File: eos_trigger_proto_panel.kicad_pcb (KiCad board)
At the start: 2 copper layers, 69.5 x 37.6 mm, 66 parts, among them J1 Conn_01x02, J2 Conn_01x02, J3 Conn_01x03, J4 Conn_01x02, U4 SMA-Mylibrary, U5 SMA-Mylibrary

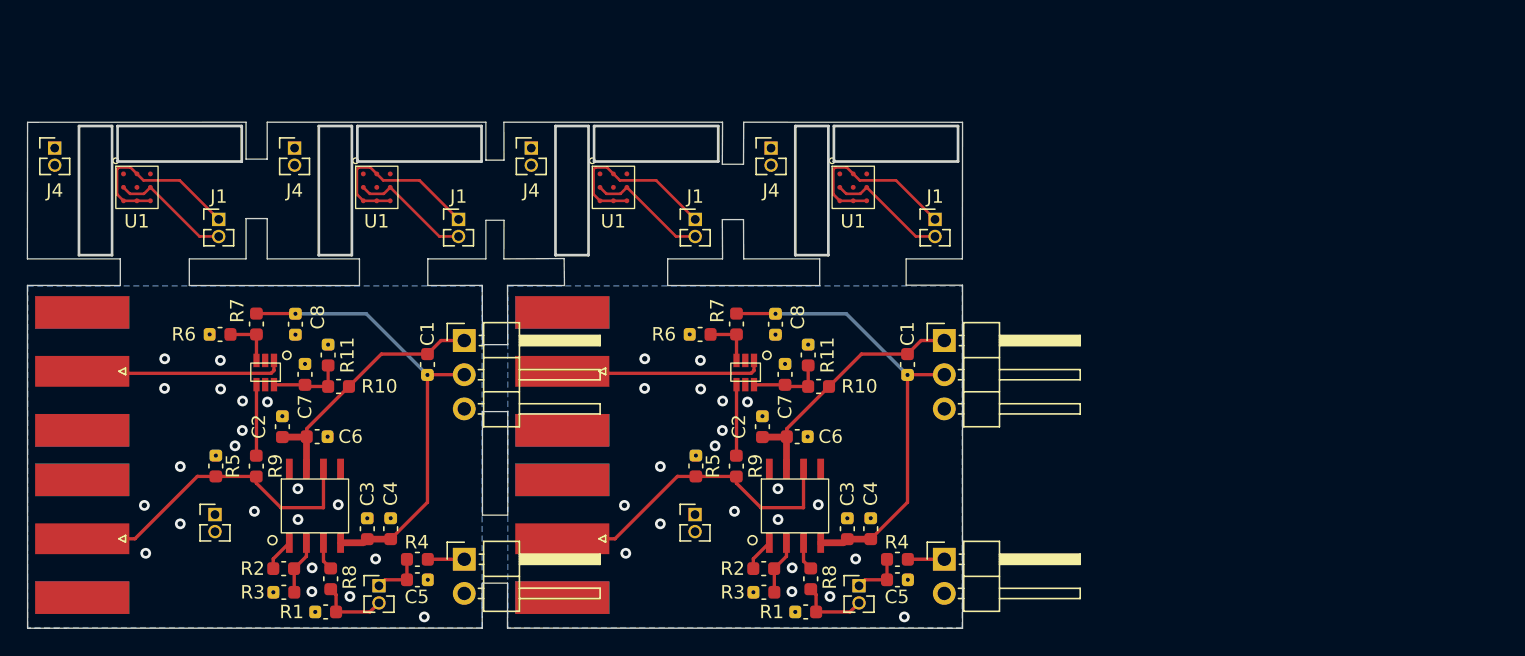
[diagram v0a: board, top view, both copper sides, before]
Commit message: update tiled panel
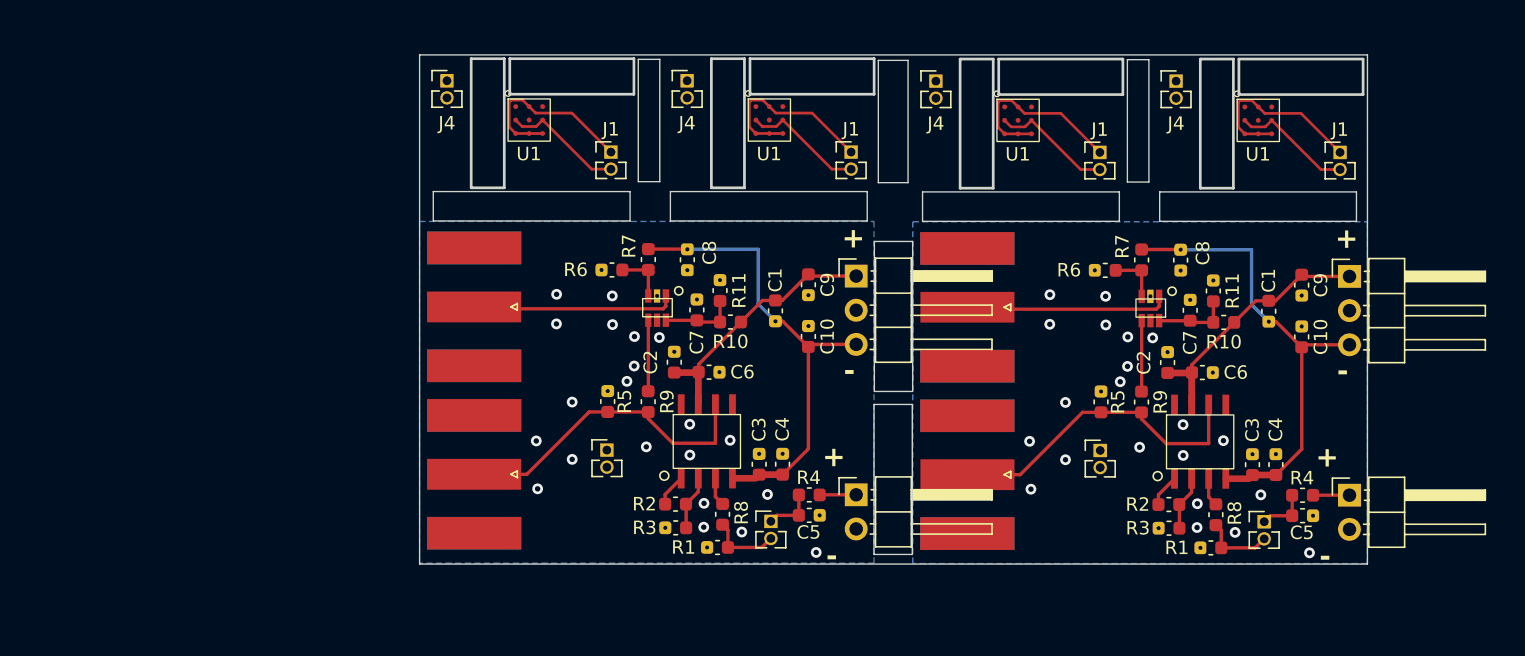
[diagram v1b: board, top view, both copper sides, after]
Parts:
- removed the C1 at (175.4, 92.9)
- removed the C1 at (139.7, 92.9)
- removed the C2 at (128.9, 97.6)
- removed the C2 at (164.6, 97.6)
- removed the C3 at (135.2, 105.2)
- removed the C3 at (170.9, 105.2)
- removed the C4 at (136.9, 105.1)
- removed the C4 at (172.6, 105.1)
- removed the C5 at (174.6, 108.9)
- removed the C5 at (138.9, 108.9)
- removed the C6 at (131.5, 98.3)
- removed the C6 at (167.2, 98.3)
- removed the C7 at (130.6, 93.7)
- removed the C7 at (166.3, 93.7)
- removed the C8 at (165.5, 89.9)
- removed the C8 at (129.9, 89.9)
- removed the J1 at (177.4, 82.2)
- removed the J1 at (124.2, 82.2)
- removed the J1 at (142.0, 82.2)
- removed the J1 at (171.8, 109.4)
- removed the J1 at (159.6, 82.2)
- removed the J1 at (136.1, 109.4)
- removed the J2 at (178.1, 107.4)
- removed the J2 at (142.4, 107.4)
- removed the J3 at (178.1, 91.2)
- removed the J3 at (142.4, 91.2)
- removed the J4 at (147.4, 76.9)
- removed the J4 at (129.8, 76.9)
- removed the J4 at (123.9, 104.1)
- removed the J4 at (159.6, 104.1)
- removed the J4 at (112.0, 76.9)
- removed the J4 at (165.2, 76.9)
- removed the R1 at (167.8, 111.3)
- removed the R1 at (132.1, 111.3)
- removed the R10 at (133.1, 94.6)
- removed the R10 at (168.8, 94.6)
- removed the R11 at (132.3, 92.2)
- removed the R11 at (168.0, 92.2)
- removed the R2 at (129.0, 108.1)
- removed the R2 at (164.7, 108.1)
- removed the R3 at (164.7, 109.9)
- removed the R3 at (129.0, 109.9)
- removed the R4 at (174.6, 107.4)
- removed the R4 at (138.9, 107.4)
- removed the R5 at (159.6, 100.5)
- removed the R5 at (123.9, 100.5)
- removed the R6 at (124.3, 90.7)
- removed the R6 at (159.9, 90.7)
- removed the R7 at (127.0, 89.9)
- removed the R7 at (162.6, 89.9)
- removed the R8 at (168.2, 108.9)
- removed the R8 at (132.5, 108.9)
- removed the R9 at (162.6, 100.5)
- removed the R9 at (127.0, 100.5)
- removed the U1 at (134.3, 78.2)
- removed the U1 at (151.9, 78.2)
- removed the U1 at (116.5, 78.2)
- removed the U1 at (169.8, 78.2)
- removed the U2 at (164.5, 101.5)
- removed the U2 at (128.8, 101.5)
- removed the U3 at (164.4, 94.2)
- removed the U3 at (128.7, 94.2)
- removed the U4 at (114.7, 105.9)
- removed the U4 at (150.4, 105.9)
- removed the U5 at (114.7, 93.5)
- removed the U5 at (150.4, 93.5)
- added C1: 0.1u, EOS_library:C_0603_1608Metric, F.Cu at (165.5, 89.0)
- added C1: 0.1u, EOS_library:C_0603_1608Metric, F.Cu at (202.2, 89.0)
- added C10: 4.7u, EOS_library:C_0603_1608Metric, F.Cu at (168.0, 90.9)
- added C10: 4.7u, EOS_library:C_0603_1608Metric, F.Cu at (204.7, 90.9)
- added C2: 10u, EOS_library:C_0603_1608Metric, F.Cu at (194.7, 92.8)
- added C2: 10u, EOS_library:C_0603_1608Metric, F.Cu at (158.0, 92.8)
- added C3: 10u, EOS_library:C_0603_1608Metric, F.Cu at (164.3, 100.4)
- added C3: 10u, EOS_library:C_0603_1608Metric, F.Cu at (201.0, 100.4)
- added C4: 0.1u, EOS_library:C_0603_1608Metric, F.Cu at (166.1, 100.4)
- added C4: 0.1u, EOS_library:C_0603_1608Metric, F.Cu at (202.7, 100.4)
- added C5: C, EOS_library:C_0603_1608Metric, F.Cu at (168.1, 104.2)
- added C5: C, EOS_library:C_0603_1608Metric, F.Cu at (204.7, 104.2)
- added C6: 0.1u, EOS_library:C_0603_1608Metric, F.Cu at (197.3, 93.5)
- added C6: 0.1u, EOS_library:C_0603_1608Metric, F.Cu at (160.6, 93.5)
- added C7: 10u, EOS_library:C_0603_1608Metric, F.Cu at (196.4, 88.9)
- added C7: 10u, EOS_library:C_0603_1608Metric, F.Cu at (159.7, 88.9)
- added C8: C, EOS_library:C_0603_1608Metric, F.Cu at (195.7, 85.2)
- added C8: C, EOS_library:C_0603_1608Metric, F.Cu at (159.0, 85.2)
- added C9: 4.7u, EOS_library:C_0603_1608Metric, F.Cu at (168.0, 87.0)
- added C9: 4.7u, EOS_library:C_0603_1608Metric, F.Cu at (204.7, 87.0)
- added J1: Conn_01x02, Connector_PinHeader_1.27mm:PinHeader_1x02_P1.27mm_Vertical, F.Cu at (207.5, 77.2)
- added J1: Conn_01x02, Connector_PinHeader_1.27mm:PinHeader_1x02_P1.27mm_Vertical, F.Cu at (153.3, 77.2)
- added J1: Conn_01x02, Connector_PinHeader_1.27mm:PinHeader_1x02_P1.27mm_Vertical, F.Cu at (189.7, 77.2)
- added J1: Conn_01x02, Connector_PinHeader_1.27mm:PinHeader_1x02_P1.27mm_Vertical, F.Cu at (201.9, 104.6)
- added J1: Conn_01x02, Connector_PinHeader_1.27mm:PinHeader_1x02_P1.27mm_Vertical, F.Cu at (165.2, 104.6)
- added J1: Conn_01x02, Connector_PinHeader_1.27mm:PinHeader_1x02_P1.27mm_Vertical, F.Cu at (171.2, 77.2)
- added J2: Conn_01x02, Connector_PinHeader_2.54mm:PinHeader_1x02_P2.54mm_Horizontal, F.Cu at (208.2, 102.7)
- added J2: Conn_01x02, Connector_PinHeader_2.54mm:PinHeader_1x02_P2.54mm_Horizontal, F.Cu at (171.5, 102.6)
- added J3: Conn_01x03, Connector_PinHeader_2.54mm:PinHeader_1x03_P2.54mm_Horizontal, F.Cu at (208.2, 86.4)
- added J3: Conn_01x03, Connector_PinHeader_2.54mm:PinHeader_1x03_P2.54mm_Horizontal, F.Cu at (171.5, 86.4)
- added J4: Conn_01x02, Connector_PinHeader_1.27mm:PinHeader_1x02_P1.27mm_Vertical, F.Cu at (141.1, 71.9)
- added J4: Conn_01x02, Connector_PinHeader_1.27mm:PinHeader_1x02_P1.27mm_Vertical, F.Cu at (153.0, 99.3)
- added J4: Conn_01x02, Connector_PinHeader_1.27mm:PinHeader_1x02_P1.27mm_Vertical, F.Cu at (177.5, 71.9)
- added J4: Conn_01x02, Connector_PinHeader_1.27mm:PinHeader_1x02_P1.27mm_Vertical, F.Cu at (159.0, 71.9)
- added J4: Conn_01x02, Connector_PinHeader_1.27mm:PinHeader_1x02_P1.27mm_Vertical, F.Cu at (195.3, 71.9)
- added J4: Conn_01x02, Connector_PinHeader_1.27mm:PinHeader_1x02_P1.27mm_Vertical, F.Cu at (189.7, 99.3)
- added R1: 49.9, EOS_library:C_0603_1608Metric, F.Cu at (197.9, 106.6)
- added R1: 49.9, EOS_library:C_0603_1608Metric, F.Cu at (161.2, 106.5)
- added R10: R, EOS_library:C_0603_1608Metric, F.Cu at (198.9, 89.8)
- added R10: R, EOS_library:C_0603_1608Metric, F.Cu at (162.2, 89.8)
- added R11: R, EOS_library:C_0603_1608Metric, F.Cu at (161.4, 87.4)
- added R11: R, EOS_library:C_0603_1608Metric, F.Cu at (198.1, 87.5)
- added R2: 499, EOS_library:C_0603_1608Metric, F.Cu at (194.8, 103.4)
- added R2: 499, EOS_library:C_0603_1608Metric, F.Cu at (158.1, 103.3)
- added R3: 13, EOS_library:C_0603_1608Metric, F.Cu at (194.8, 105.1)
- added R3: 13, EOS_library:C_0603_1608Metric, F.Cu at (158.1, 105.1)
- added R4: R, EOS_library:C_0603_1608Metric, F.Cu at (168.1, 102.6)
- added R4: R, EOS_library:C_0603_1608Metric, F.Cu at (204.7, 102.7)
- added R5: 49.9, EOS_library:C_0603_1608Metric, F.Cu at (153.1, 95.7)
- added R5: 49.9, EOS_library:C_0603_1608Metric, F.Cu at (189.7, 95.7)
- added R6: R, EOS_library:C_0603_1608Metric, F.Cu at (190.1, 85.9)
- added R6: R, EOS_library:C_0603_1608Metric, F.Cu at (153.4, 85.9)
- added R7: R, EOS_library:C_0603_1608Metric, F.Cu at (192.8, 85.2)
- added R7: R, EOS_library:C_0603_1608Metric, F.Cu at (156.1, 85.1)
- added R8: 0, EOS_library:C_0603_1608Metric, F.Cu at (161.6, 104.1)
- added R8: 0, EOS_library:C_0603_1608Metric, F.Cu at (198.3, 104.1)
- added R9: 0, EOS_library:C_0603_1608Metric, F.Cu at (156.1, 95.7)
- added R9: 0, EOS_library:C_0603_1608Metric, F.Cu at (192.8, 95.7)
- added U1: ~, EOS_library:AFBR-S4N33C013, F.Cu at (199.9, 73.2)
- added U1: ~, EOS_library:AFBR-S4N33C013, F.Cu at (145.7, 73.2)
- added U1: ~, EOS_library:AFBR-S4N33C013, F.Cu at (182.0, 73.2)
- added U1: ~, EOS_library:AFBR-S4N33C013, F.Cu at (163.5, 73.2)
- added U2: AD8099, EOS_library:AD8099, F.Cu at (194.6, 96.7)
- added U2: AD8099, EOS_library:AD8099, F.Cu at (157.9, 96.7)
- added U3: LTC6752-1, EOS_library:LT6752-1, F.Cu at (194.5, 89.4)
- added U3: LTC6752-1, EOS_library:LT6752-1, F.Cu at (157.9, 89.4)
- added U4: SMA-Mylibrary, EOS_library:SMA_Molex_73251-1153_EdgeMount_Horizontal, F.Cu at (180.5, 101.1)
- added U4: SMA-Mylibrary, EOS_library:SMA_Molex_73251-1153_EdgeMount_Horizontal, F.Cu at (143.9, 101.1)
- added U5: SMA-Mylibrary, EOS_library:SMA_Molex_73251-1153_EdgeMount_Horizontal, F.Cu at (143.9, 88.7)
- added U5: SMA-Mylibrary, EOS_library:SMA_Molex_73251-1153_EdgeMount_Horizontal, F.Cu at (180.5, 88.7)
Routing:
- net -5V: track 68.3 -> 69.3 mm
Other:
- board size 69.5 x 37.6 mm -> 70.5 x 37.8 mm
- board text added: "+"
- board text added: "-"

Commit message: tweaks
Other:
- board size 70.5 x 37.8 mm -> 70.8 x 38.2 mm
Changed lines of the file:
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@@
   (gr_rect (start 182.1418 70.2336) (end 191.3718 72.8736)
     (stroke (width 0.2) (type default)) (fill none) (layer "Edge.Cuts"))
-  (gr_rect (start 191.7065 70.2818) (end 193.3067 79.375)
-    (stroke (width 0.1) (type default)) (fill none) (layer "Edge.Cuts"))
-  (gr_rect (start 172.8724 95.9104) (end 175.7172 107.061)
-    (stroke (width 0.1) (type default)) (fill none) (layer "Edge.Cuts"))
   (gr_rect (start 199.998 70.2336) (end 209.228 72.8736)
     (stroke (width 0.2) (type default)) (fill none) (layer "Edge.Cuts"))
   (gr_rect (start 160.7806 70.2082) (end 163.2406 79.8082)
     (stroke (width 0.2) (type default)) (fill none) (layer "Edge.Cuts"))
-  (gr_rect (start 140.1064 80.0862) (end 154.7368 82.2706)
-    (stroke (width 0.1) (type default)) (fill none) (layer "Edge.Cuts"))
-  (gr_rect (start 155.3464 70.2564) (end 156.9466 79.3496)
-    (stroke (width 0.1) (type default)) (fill none) (layer "Edge.Cuts"))
+  (gr_rect (start 139.446 80.2894) (end 155.829 82.1182)
+    (stroke (width 0.2) (type default)) (fill none) (layer "Edge.Cuts"))
+  (gr_rect (start 191.8716 70.231) (end 193.3448 79.8322)
+    (stroke (width 0.2) (type default)) (fill none) (layer "Edge.Cuts"))
+  (gr_rect (start 155.4734 70.2056) (end 156.9466 79.6544)
+    (stroke (width 0.2) (type default)) (fill none) (layer "Edge.Cuts"))
   (gr_rect (start 163.6506 70.2082) (end 172.8806 72.8482)
     (stroke (width 0.2) (type default)) (fill none) (layer "Edge.Cuts"))
-  (gr_rect (start 176.4792 80.1116) (end 191.1096 82.296)
-    (stroke (width 0.1) (type default)) (fill none) (layer "Edge.Cuts"))
-  (gr_rect (start 139.0904 69.9262) (end 209.5536 107.776)
-    (stroke (width 0.1) (type default)) (fill none) (layer "Edge.Cuts"))
-  (gr_rect (start 172.8978 83.7946) (end 175.7426 94.9452)
-    (stroke (width 0.1) (type default)) (fill none) (layer "Edge.Cuts"))
+  (gr_rect (start 138.9126 69.7738) (end 209.7278 107.95)
+    (stroke (width 0.2) (type default)) (fill none) (layer "Edge.Cuts"))
+  (gr_rect (start 174.7266 80.264) (end 192.2526 82.0928)
+    (stroke (width 0.2) (type default)) (fill none) (layer "Edge.Cuts"))
+  (gr_rect (start 192.9892 80.264) (end 209.1436 82.1182)
+    (stroke (width 0.2) (type default)) (fill none) (layer "Edge.Cuts"))
+  (gr_rect (start 173.1264 82.4992) (end 175.5394 94.9452)
+    (stroke (width 0.2) (type default)) (fill none) (layer "Edge.Cuts"))
   (gr_rect (start 145.7944 70.2082) (end 155.0244 72.8482)
     (stroke (width 0.2) (type default)) (fill none) (layer "Edge.Cuts"))
-  (gr_rect (start 157.734 80.0862) (end 172.3644 82.2706)
-    (stroke (width 0.1) (type default)) (fill none) (layer "Edge.Cuts"))
-  (gr_rect (start 173.1899 70.3326) (end 175.3997 79.4258)
-    (stroke (width 0.1) (type default)) (fill none) (layer "Edge.Cuts"))
-  (gr_rect (start 194.1068 80.1116) (end 208.7372 82.296)
-    (stroke (width 0.1) (type default)) (fill none) (layer "Edge.Cuts"))
+  (gr_rect (start 173.3423 70.2056) (end 175.2981 79.8322)
+    (stroke (width 0.2) (type default)) (fill none) (layer "Edge.Cuts"))
+  (gr_rect (start 156.6418 80.264) (end 173.9392 82.0928)
+    (stroke (width 0.2) (type default)) (fill none) (layer "Edge.Cuts"))
   (gr_rect (start 142.9244 70.2082) (end 145.3844 79.8082)
     (stroke (width 0.2) (type default)) (fill none) (layer "Edge.Cuts"))
+  (gr_rect (start 173.1264 95.4786) (end 175.5394 107.4166)
+    (stroke (width 0.2) (type default)) (fill none) (layer "Edge.Cuts"))
   (gr_rect (start 179.2718 70.2336) (end 181.7318 79.8336)

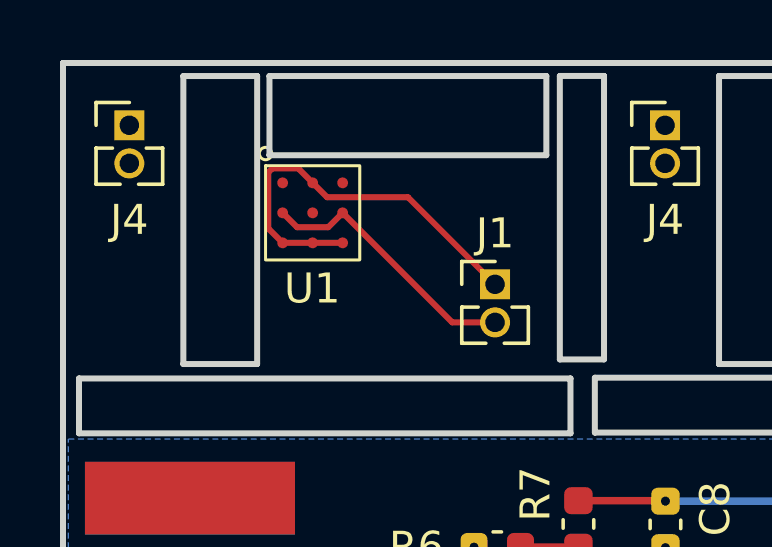
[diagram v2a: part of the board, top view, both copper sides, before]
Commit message: update pin connector size
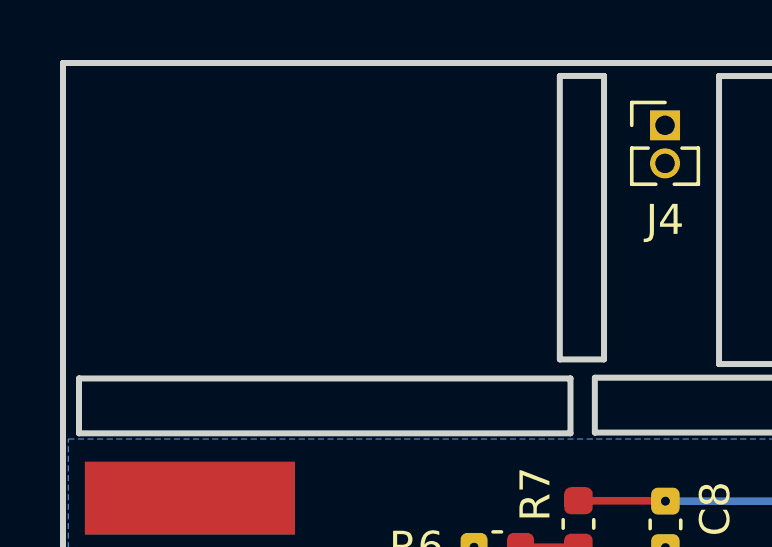
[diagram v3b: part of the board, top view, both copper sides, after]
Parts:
- removed the J1 at (153.3, 77.2)
- removed the J4 at (141.1, 71.9)
- removed the U1 at (145.7, 73.2)
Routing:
- net /IN: track 55.0 -> 41.3 mm
- net /OUT: track 36.0 -> 27.0 mm
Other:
- outline, holes or cut-outs redrawn

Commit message: update panel
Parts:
- removed the C1 at (165.5, 89.0)
- removed the C1 at (202.2, 89.0)
- removed the C10 at (168.0, 90.9)
- removed the C10 at (204.7, 90.9)
- removed the C2 at (194.7, 92.8)
- removed the C2 at (158.0, 92.8)
- removed the C3 at (164.3, 100.4)
- removed the C3 at (201.0, 100.4)
- removed the C4 at (166.1, 100.4)
- removed the C4 at (202.7, 100.4)
- removed the C5 at (168.1, 104.2)
- removed the C5 at (204.7, 104.2)
- removed the C6 at (197.3, 93.5)
- removed the C6 at (160.6, 93.5)
- removed the C7 at (196.4, 88.9)
- removed the C7 at (159.7, 88.9)
- removed the C8 at (195.7, 85.2)
- removed the C8 at (159.0, 85.2)
- removed the C9 at (168.0, 87.0)
- removed the C9 at (204.7, 87.0)
- removed the J1 at (207.5, 77.2)
- removed the J1 at (189.7, 77.2)
- removed the J1 at (201.9, 104.6)
- removed the J1 at (165.2, 104.6)
- removed the J1 at (171.2, 77.2)
- removed the J2 at (208.2, 102.7)
- removed the J2 at (171.5, 102.6)
- removed the J3 at (208.2, 86.4)
- removed the J3 at (171.5, 86.4)
- removed the J4 at (153.0, 99.3)
- removed the J4 at (177.5, 71.9)
- removed the J4 at (159.0, 71.9)
- removed the J4 at (195.3, 71.9)
- removed the J4 at (189.7, 99.3)
- removed the R1 at (197.9, 106.6)
- removed the R1 at (161.2, 106.5)
- removed the R10 at (198.9, 89.8)
- removed the R10 at (162.2, 89.8)
- removed the R11 at (161.4, 87.4)
- removed the R11 at (198.1, 87.5)
- removed the R2 at (194.8, 103.4)
- removed the R2 at (158.1, 103.3)
- removed the R3 at (194.8, 105.1)
- removed the R3 at (158.1, 105.1)
- removed the R4 at (168.1, 102.6)
- removed the R4 at (204.7, 102.7)
- removed the R5 at (153.1, 95.7)
- removed the R5 at (189.7, 95.7)
- removed the R6 at (190.1, 85.9)
- removed the R6 at (153.4, 85.9)
- removed the R7 at (192.8, 85.2)
- removed the R7 at (156.1, 85.1)
- removed the R8 at (161.6, 104.1)
- removed the R8 at (198.3, 104.1)
- removed the R9 at (156.1, 95.7)
- removed the R9 at (192.8, 95.7)
- removed the U1 at (199.9, 73.2)
- removed the U1 at (182.0, 73.2)
- removed the U1 at (163.5, 73.2)
- removed the U2 at (194.6, 96.7)
- removed the U2 at (157.9, 96.7)
- removed the U3 at (194.5, 89.4)
- removed the U3 at (157.9, 89.4)
- removed the U4 at (180.5, 101.1)
- removed the U4 at (143.9, 101.1)
- removed the U5 at (143.9, 88.7)
- removed the U5 at (180.5, 88.7)
- added C1: 0.1u, EOS_library:C_0603_1608Metric, F.Cu at (203.1, 88.9)
- added C1: 0.1u, EOS_library:C_0603_1608Metric, F.Cu at (164.8, 89.0)
- added C10: 4.7u, EOS_library:C_0603_1608Metric, F.Cu at (167.3, 90.9)
- added C10: 4.7u, EOS_library:C_0603_1608Metric, F.Cu at (205.5, 90.8)
- added C2: 10u, EOS_library:C_0603_1608Metric, F.Cu at (157.3, 92.9)
- added C2: 10u, EOS_library:C_0603_1608Metric, F.Cu at (195.6, 92.8)
- added C3: 10u, EOS_library:C_0603_1608Metric, F.Cu at (201.9, 98.5)
- added C3: 10u, EOS_library:C_0603_1608Metric, F.Cu at (163.6, 98.6)
- added C4: 0.1u, EOS_library:C_0603_1608Metric, F.Cu at (165.3, 98.6)
- added C4: 0.1u, EOS_library:C_0603_1608Metric, F.Cu at (203.6, 98.5)
- added C5: C, EOS_library:C_0603_1608Metric, F.Cu at (167.3, 104.2)
- added C5: C, EOS_library:C_0603_1608Metric, F.Cu at (205.6, 104.1)
- added C6: 0.1u, EOS_library:C_0603_1608Metric, F.Cu at (159.9, 93.6)
- added C6: 0.1u, EOS_library:C_0603_1608Metric, F.Cu at (198.2, 93.5)
- added C7: 10u, EOS_library:C_0603_1608Metric, F.Cu at (159.0, 89.0)
- added C7: 10u, EOS_library:C_0603_1608Metric, F.Cu at (197.2, 88.9)
- added C8: C, EOS_library:C_0603_1608Metric, F.Cu at (196.5, 85.1)
- added C8: C, EOS_library:C_0603_1608Metric, F.Cu at (158.3, 85.2)
- added C9: 4.7u, EOS_library:C_0603_1608Metric, F.Cu at (167.3, 87.1)
- added C9: 4.7u, EOS_library:C_0603_1608Metric, F.Cu at (205.5, 87.0)
- added J1: Conn_01x02, Connector_PinHeader_2.54mm:PinHeader_1x02_P2.54mm_Vertical, F.Cu at (202.2, 103.2)
- added J1: Conn_01x02, Connector_PinHeader_2.54mm:PinHeader_1x02_P2.54mm_Vertical, F.Cu at (152.3, 75.5)
- added J1: Conn_01x02, Connector_PinHeader_2.54mm:PinHeader_1x02_P2.54mm_Vertical, F.Cu at (208.3, 75.5)
- added J1: Conn_01x02, Connector_PinHeader_2.54mm:PinHeader_1x02_P2.54mm_Vertical, F.Cu at (171.0, 75.5)
- added J1: Conn_01x02, Connector_PinHeader_2.54mm:PinHeader_1x02_P2.54mm_Vertical, F.Cu at (164.0, 103.3)
- added J1: Conn_01x02, Connector_PinHeader_2.54mm:PinHeader_1x02_P2.54mm_Vertical, F.Cu at (189.7, 75.5)
- added J2: Conn_01x02, Connector_PinHeader_2.54mm:PinHeader_1x02_P2.54mm_Horizontal, F.Cu at (170.8, 102.7)
- added J2: Conn_01x02, Connector_PinHeader_2.54mm:PinHeader_1x02_P2.54mm_Horizontal, F.Cu at (209.1, 102.6)
- added J3: Conn_01x03, Connector_PinHeader_2.54mm:PinHeader_1x03_P2.54mm_Horizontal, F.Cu at (170.8, 86.5)
- added J3: Conn_01x03, Connector_PinHeader_2.54mm:PinHeader_1x03_P2.54mm_Horizontal, F.Cu at (209.1, 86.4)
- added J4: Conn_01x02, Connector_PinHeader_2.54mm:PinHeader_1x02_P2.54mm_Vertical, F.Cu at (158.8, 70.2)
- added J4: Conn_01x02, Connector_PinHeader_2.54mm:PinHeader_1x02_P2.54mm_Vertical, F.Cu at (140.1, 70.2)
- added J4: Conn_01x02, Connector_PinHeader_2.54mm:PinHeader_1x02_P2.54mm_Vertical, F.Cu at (196.1, 70.2)
- added J4: Conn_01x02, Connector_PinHeader_2.54mm:PinHeader_1x02_P2.54mm_Vertical, F.Cu at (151.7, 98.0)
- added J4: Conn_01x02, Connector_PinHeader_2.54mm:PinHeader_1x02_P2.54mm_Vertical, F.Cu at (177.5, 70.2)
- added J4: Conn_01x02, Connector_PinHeader_2.54mm:PinHeader_1x02_P2.54mm_Vertical, F.Cu at (190.0, 97.9)
- added R1: 49.9, EOS_library:C_0603_1608Metric, F.Cu at (198.8, 106.5)
- added R1: 49.9, EOS_library:C_0603_1608Metric, F.Cu at (160.5, 106.6)
- added R10: R, EOS_library:C_0603_1608Metric, F.Cu at (161.5, 89.9)
- added R10: R, EOS_library:C_0603_1608Metric, F.Cu at (199.7, 89.8)
- added R11: R, EOS_library:C_0603_1608Metric, F.Cu at (199.0, 87.4)
- added R11: R, EOS_library:C_0603_1608Metric, F.Cu at (160.7, 87.5)
- added R2: 499, EOS_library:C_0603_1608Metric, F.Cu at (195.7, 103.3)
- added R2: 499, EOS_library:C_0603_1608Metric, F.Cu at (157.4, 103.4)
- added R3: 13, EOS_library:C_0603_1608Metric, F.Cu at (195.7, 105.1)
- added R3: 13, EOS_library:C_0603_1608Metric, F.Cu at (157.4, 105.2)
- added R4: R, EOS_library:C_0603_1608Metric, F.Cu at (167.3, 102.7)
- added R4: R, EOS_library:C_0603_1608Metric, F.Cu at (205.6, 102.6)
- added R5: 49.9, EOS_library:C_0603_1608Metric, F.Cu at (151.6, 104.4)
- added R5: 49.9, EOS_library:C_0603_1608Metric, F.Cu at (189.9, 104.3)
- added R6: R, EOS_library:C_0603_1608Metric, F.Cu at (190.9, 85.9)
- added R6: R, EOS_library:C_0603_1608Metric, F.Cu at (152.7, 86.0)
- added R7: R, EOS_library:C_0603_1608Metric, F.Cu at (155.4, 85.2)
- added R7: R, EOS_library:C_0603_1608Metric, F.Cu at (193.6, 85.1)
- added R8: 0, EOS_library:C_0603_1608Metric, F.Cu at (199.2, 104.1)
- added R8: 0, EOS_library:C_0603_1608Metric, F.Cu at (160.9, 104.2)
- added R9: 0, EOS_library:C_0603_1608Metric, F.Cu at (155.3, 95.8)
- added R9: 0, EOS_library:C_0603_1608Metric, F.Cu at (193.6, 95.7)
- added U1: ~, EOS_library:AFBR-S4N33C013, F.Cu at (182.2, 72.6)
- added U1: ~, EOS_library:AFBR-S4N33C013, F.Cu at (163.5, 72.6)
- added U1: ~, EOS_library:AFBR-S4N33C013, F.Cu at (144.8, 72.6)
- added U1: ~, EOS_library:AFBR-S4N33C013, F.Cu at (200.8, 72.6)
- added U2: AD8099, EOS_library:AD8099, F.Cu at (157.2, 96.8)
- added U2: AD8099, EOS_library:AD8099, F.Cu at (195.5, 96.7)
- added U3: LTC6752-1, EOS_library:LT6752-1, F.Cu at (195.4, 89.4)
- added U3: LTC6752-1, EOS_library:LT6752-1, F.Cu at (157.1, 89.5)
- added U4: SMA-Mylibrary, EOS_library:SMA_Molex_73251-1153_EdgeMount_Horizontal, F.Cu at (143.1, 101.2)
- added U4: SMA-Mylibrary, EOS_library:SMA_Molex_73251-1153_EdgeMount_Horizontal, F.Cu at (181.4, 101.1)
- added U5: SMA-Mylibrary, EOS_library:SMA_Molex_73251-1153_EdgeMount_Horizontal, F.Cu at (181.4, 88.6)
- added U5: SMA-Mylibrary, EOS_library:SMA_Molex_73251-1153_EdgeMount_Horizontal, F.Cu at (143.1, 88.7)
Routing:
- net /IN: track 41.3 -> 52.6 mm
- net SIG OUT: track 48.0 -> 57.2 mm
- net /OUT: track 27.0 -> 35.6 mm
- net GND: track 0.00 -> 8.54 mm, vias 42 -> 32
- net /SiPM_daughter/OUT: track 10.6 -> 3.71 mm
- net -5V: track 69.3 -> 68.1 mm
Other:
- board size 70.8 x 38.2 mm -> 72.9 x 40.1 mm
